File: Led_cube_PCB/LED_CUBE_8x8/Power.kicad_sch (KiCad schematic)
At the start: 12 parts, among them IC28 TPS562202DRLR

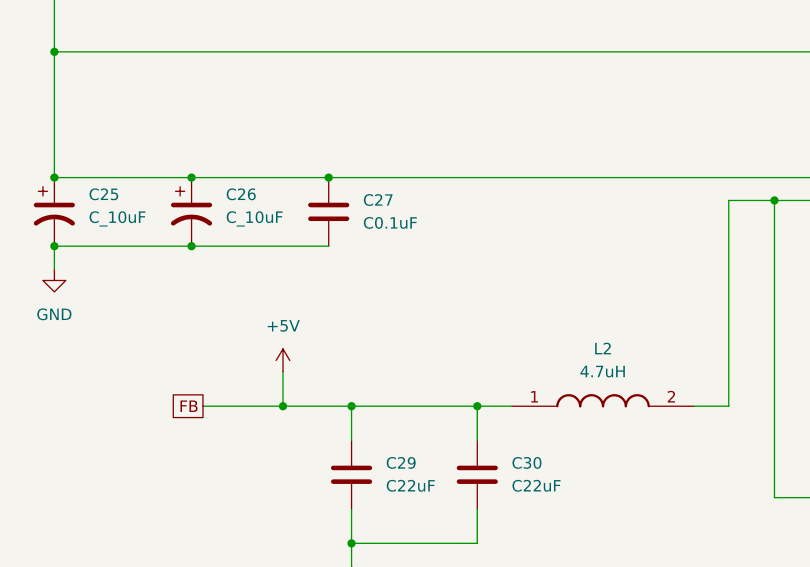
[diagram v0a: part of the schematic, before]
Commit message: added 3.3V power supply for microcontroller and started on STM schematic.
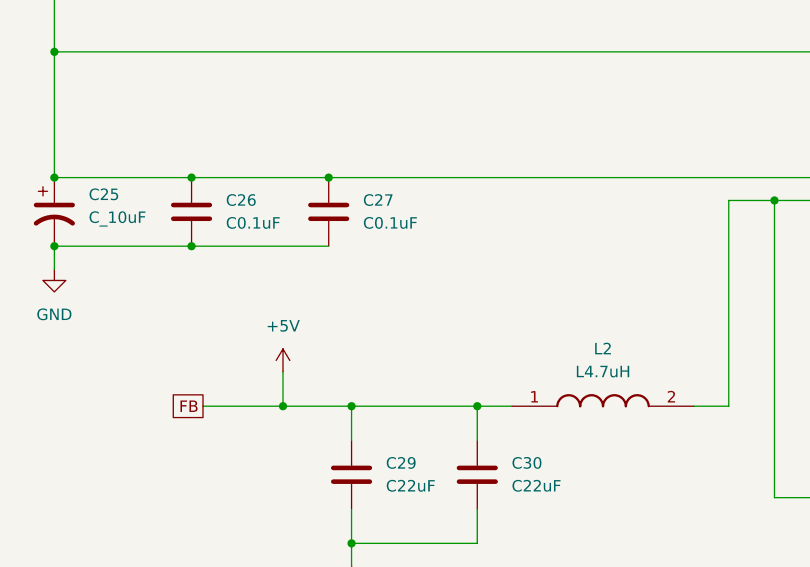
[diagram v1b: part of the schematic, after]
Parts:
- removed C26: C_10uF, symbol Device:C_Polarized_US
- added C26: C0.1uF, symbol Device:C
- L2: value 4.7uH -> L4.7uH
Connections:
- net +12V: now also C26.1
- net GND: now also C26.2

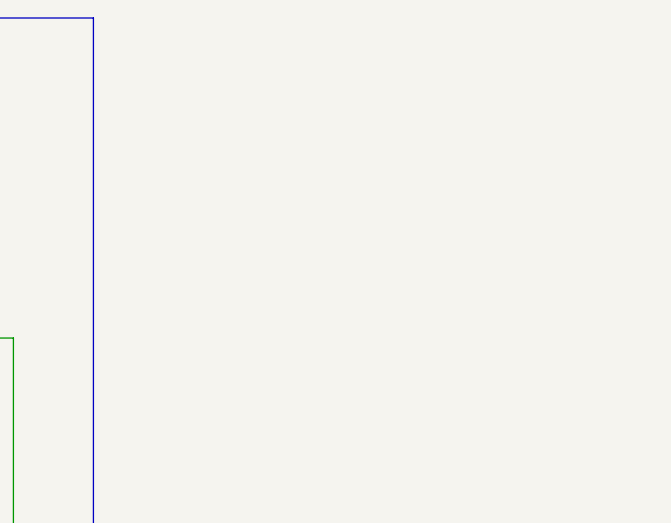
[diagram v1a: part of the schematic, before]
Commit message: WIP: need to add connectors for the LED channels
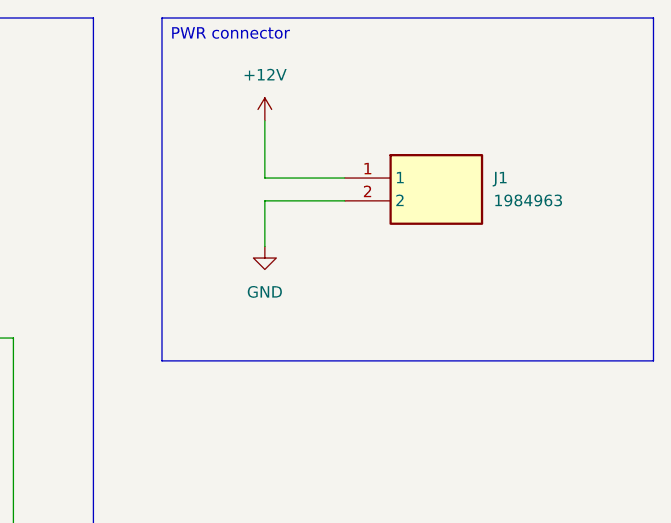
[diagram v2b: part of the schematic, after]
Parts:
- added J1: 1984963, 1984963, symbol SamacSys_Parts:1984963
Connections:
- net +12V: now also J1.1
- net GND: now also J1.2
